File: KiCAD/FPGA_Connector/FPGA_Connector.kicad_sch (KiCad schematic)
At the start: 1 part, among them J1 AHDF15A-KG-TAXB

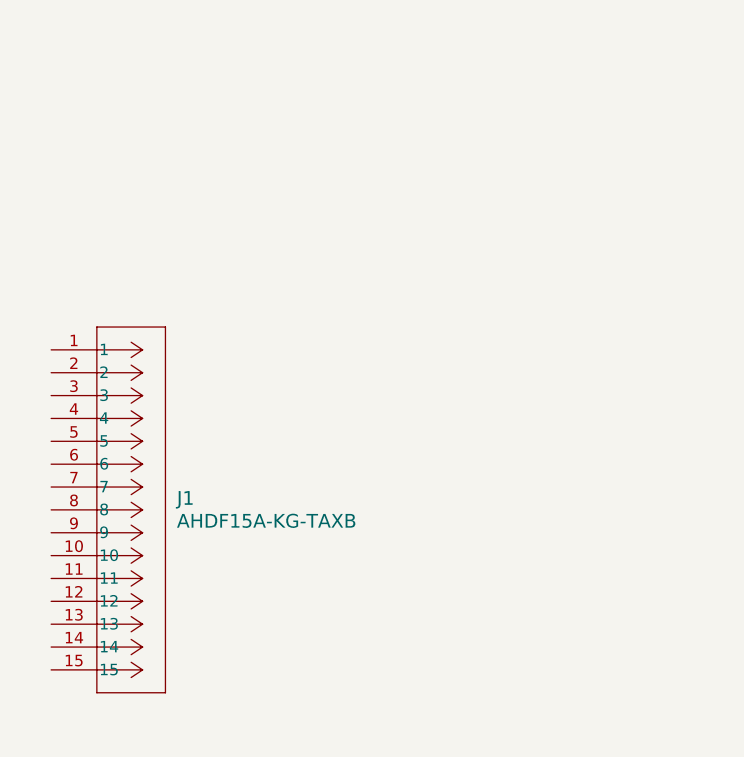
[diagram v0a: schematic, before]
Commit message: Added our connector board from FPGA to main board
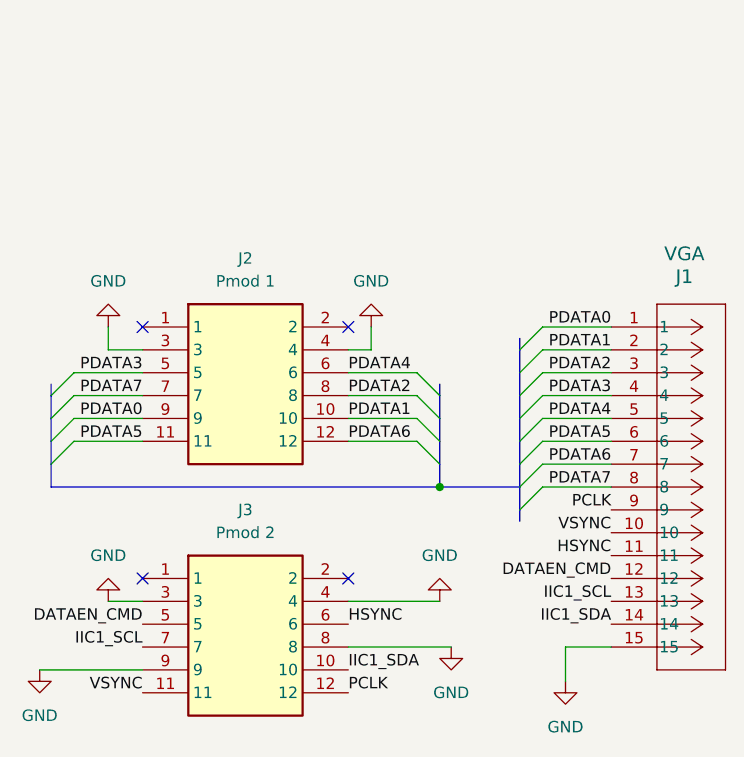
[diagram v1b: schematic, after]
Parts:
- added J2: Pmod 1, horizontalHeader:HDRRA12W63P254_2X6_1514X280X635P, symbol 2x6horizontalHeaders:825457-6
- added J3: Pmod 2, horizontalHeader:HDRRA12W63P254_2X6_1514X280X635P, symbol 2x6horizontalHeaders:825457-6
- J1: value AHDF15A-KG-TAXB -> VGA
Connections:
- net PDATA0: now reaches J1.1
- net PDATA0: now also J2.9
- net VSYNC: now reaches J1.10
- net VSYNC: now also J3.11
- net HSYNC: now reaches J1.11
- net HSYNC: now also J3.6
- net DATAEN_CMD: now reaches J1.12
- net DATAEN_CMD: now also J3.5
- net IIC1_SCL: now reaches J1.13
- net IIC1_SCL: now also J3.7
- net IIC1_SDA: now reaches J1.14
- net IIC1_SDA: now also J3.10
- net GND: now reaches J1.15
- net GND: now also J2.3, J2.4, J3.3, J3.4, J3.8, J3.9
- net PDATA1: now reaches J1.2
- net PDATA1: now also J2.10
- net PDATA2: now reaches J1.3
- net PDATA2: now also J2.8
- net PDATA3: now reaches J1.4
- net PDATA3: now also J2.5
- net PDATA4: now reaches J1.5
- net PDATA4: now also J2.6
- net PDATA5: now reaches J1.6
- net PDATA5: now also J2.11
- net PDATA6: now reaches J1.7
- net PDATA6: now also J2.12
- net PDATA7: now reaches J1.8
- net PDATA7: now also J2.7
- net PCLK: now reaches J1.9
- net PCLK: now also J3.12
- no-connect marks 0 -> 4
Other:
- moved on the sheet: J1

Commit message: added 3d models to FPGA Board
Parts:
- J1: footprint footprints:CONN_AHDF15A-KG-TAXB_ASM -> footprints:AHDF15AKGTAXB
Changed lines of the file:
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@@
 			)
 		)
-		(property "Footprint" "footprints:CONN_AHDF15A-KG-TAXB_ASM"
+		(property "Footprint" "footprints:AHDF15AKGTAXB"
 			(at 166.116 65.786 0)
 			(effects

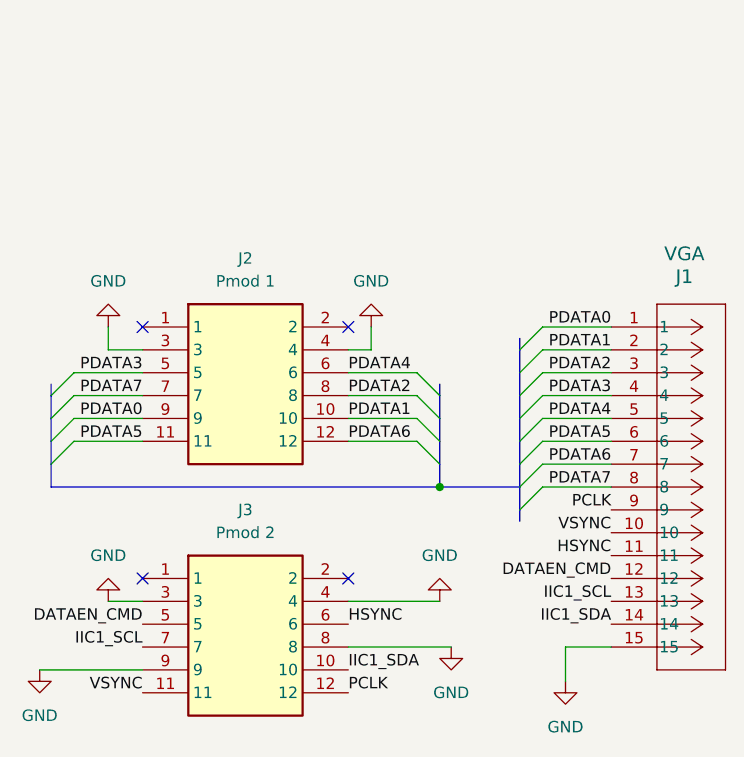
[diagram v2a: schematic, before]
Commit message: fixed bus connection on fpga connector
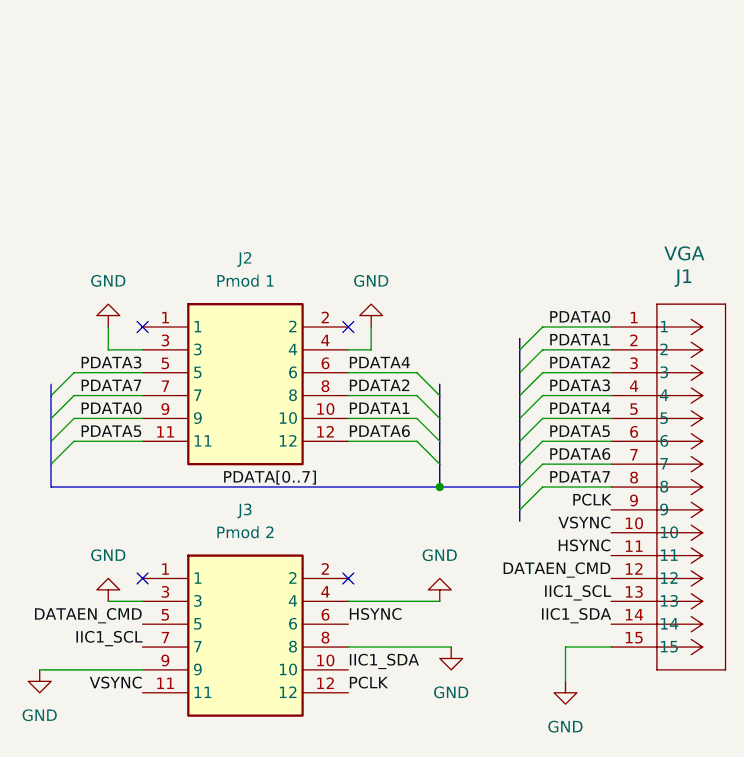
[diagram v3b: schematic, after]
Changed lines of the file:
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@@
+		)
+	)
+	(label "PDATA[0..7]"
+		(at 124.46 87.63 0)
+		(effects
+			(font
+				(size 1.27 1.27)
+			)
+			(justify left bottom)
 		)
 	)

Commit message: fixed all proj specific compoents
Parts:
- added J4: Conn_02x06_Counter_Clockwise, Connector_PinHeader_2.54mm:PinHeader_2x06_P2.54mm_Horizontal, symbol Connector_Generic:Conn_02x06_Counter_Clockwise
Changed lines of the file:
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@@
+	)
+	(symbol
+		(lib_id "Connector_Generic:Conn_02x06_Counter_Clockwise")
+		(at 123.19 48.26 0)
+		(unit 1)
+		(exclude_from_sim no)
+		(in_bom yes)
+		(on_board yes)
+		(dnp no)
+		(fields_autoplaced yes)
+		(property "Reference" "J4"
+			(at 124.46 36.83 0)
+			(effects
+				(font
+					(size 1.27 1.27)
+				)
+			)
+		)
+		(property "Value" "Conn_02x06_Counter_Clockwise"
+			(at 124.46 39.37 0)
+			(effects
+				(font
+					(size 1.27 1.27)
+				)
+			)
+		)
+		(property "Footprint" "Connector_PinHeader_2.54mm:PinHeader_2x06_P2.54mm_Horizontal"
+			(at 123.19 48.26 0)
+			(effects
+				(font
+					(size 1.27 1.27)
+				)
+				(hide yes)
+			)
+		)
+		(property "Datasheet" "~"
+			(at 123.19 48.26 0)
+			(effects
+				(font
+					(size 1.27 1.27)
+				)
+				(hide yes)
+			)
+		)
+		(property "Description" "Generic connector, double row, 02x06, counter clockwise pin numbering scheme (similar to DIP package numbering), script generated (kicad-library-utils/schlib/autogen/connector/)"
+			(at 123.19 48.26 0)
+			(effects
+				(font
+					(size 1.27 1.27)
+				)
+				(hide yes)
+			)
+		)
+		(pin "4"
+		)
+		(pin "10"
+		)
+		(pin "5"
+		)
+		(pin "11"
+		)
+		(pin "6"
+		)
+		(pin "1"
+		)
+		(pin "2"
+		)
+		(pin "3"
+		)
+		(pin "12"
+		)
+		(pin "9"
+		)
+		(pin "8"
+		)
+		(pin "7"
+		)
+		(instances
+			(project ""
+				(path "/ea18f202-f160-4b0d-b44c-7a846953c9b1"
+					(reference "J4")
+					(unit 1)
+				)
+			)
+		)
 	)
 	(symbol
